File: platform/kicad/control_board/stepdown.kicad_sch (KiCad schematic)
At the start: 7 parts, among them U3 AP63205WU-7

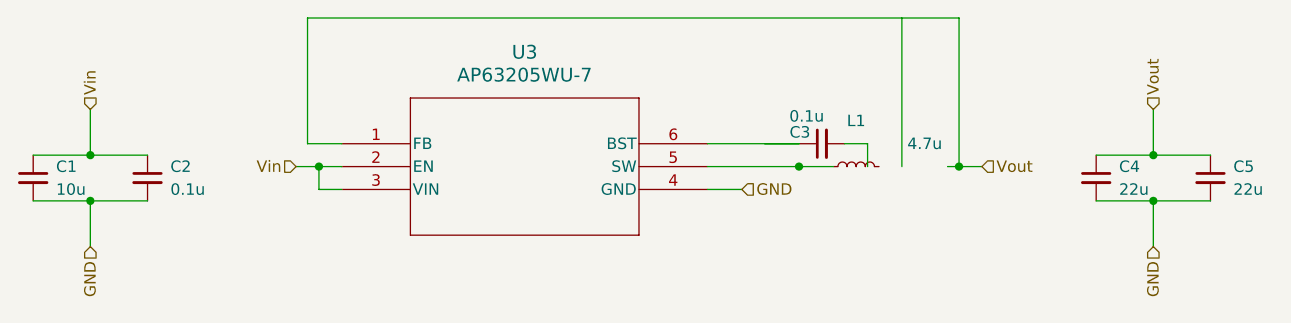
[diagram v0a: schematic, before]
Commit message: Controller: Finalise for production
This change updates the production files
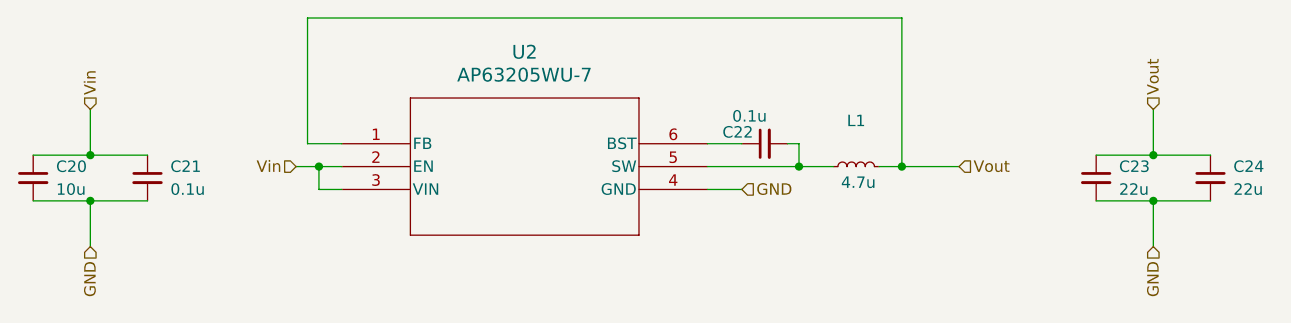
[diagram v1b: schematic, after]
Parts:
- L1: footprint AusOcean:WE-XHMI_6060 -> Inductor_SMD:L_Changjiang_FXL0630
- renumbered C1 to C20, C2 to C21, C3 to C22, C4 to C23, C5 to C24, U3 to U2
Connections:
- net Vout: now also L1.2
- net at C22.2: now also L1.1, U2.5 (SW)
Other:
- moved on the sheet: C22
